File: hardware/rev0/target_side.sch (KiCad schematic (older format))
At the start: 4 parts, among them IC1 ECP5-BGA256

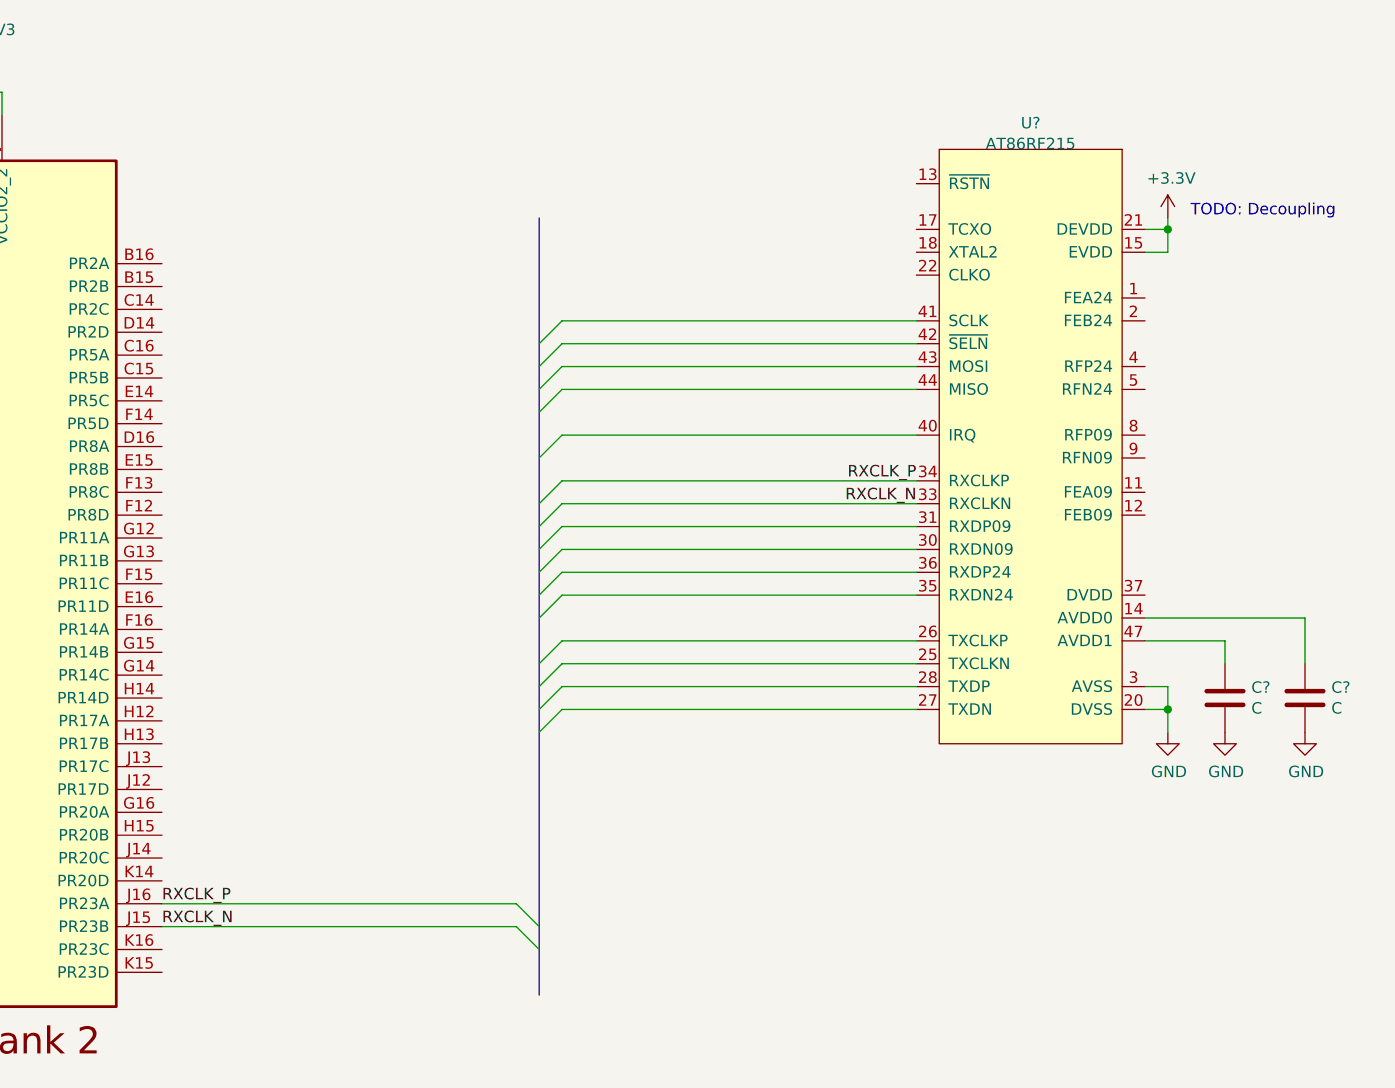
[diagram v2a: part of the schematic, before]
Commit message: Rough out LVDS
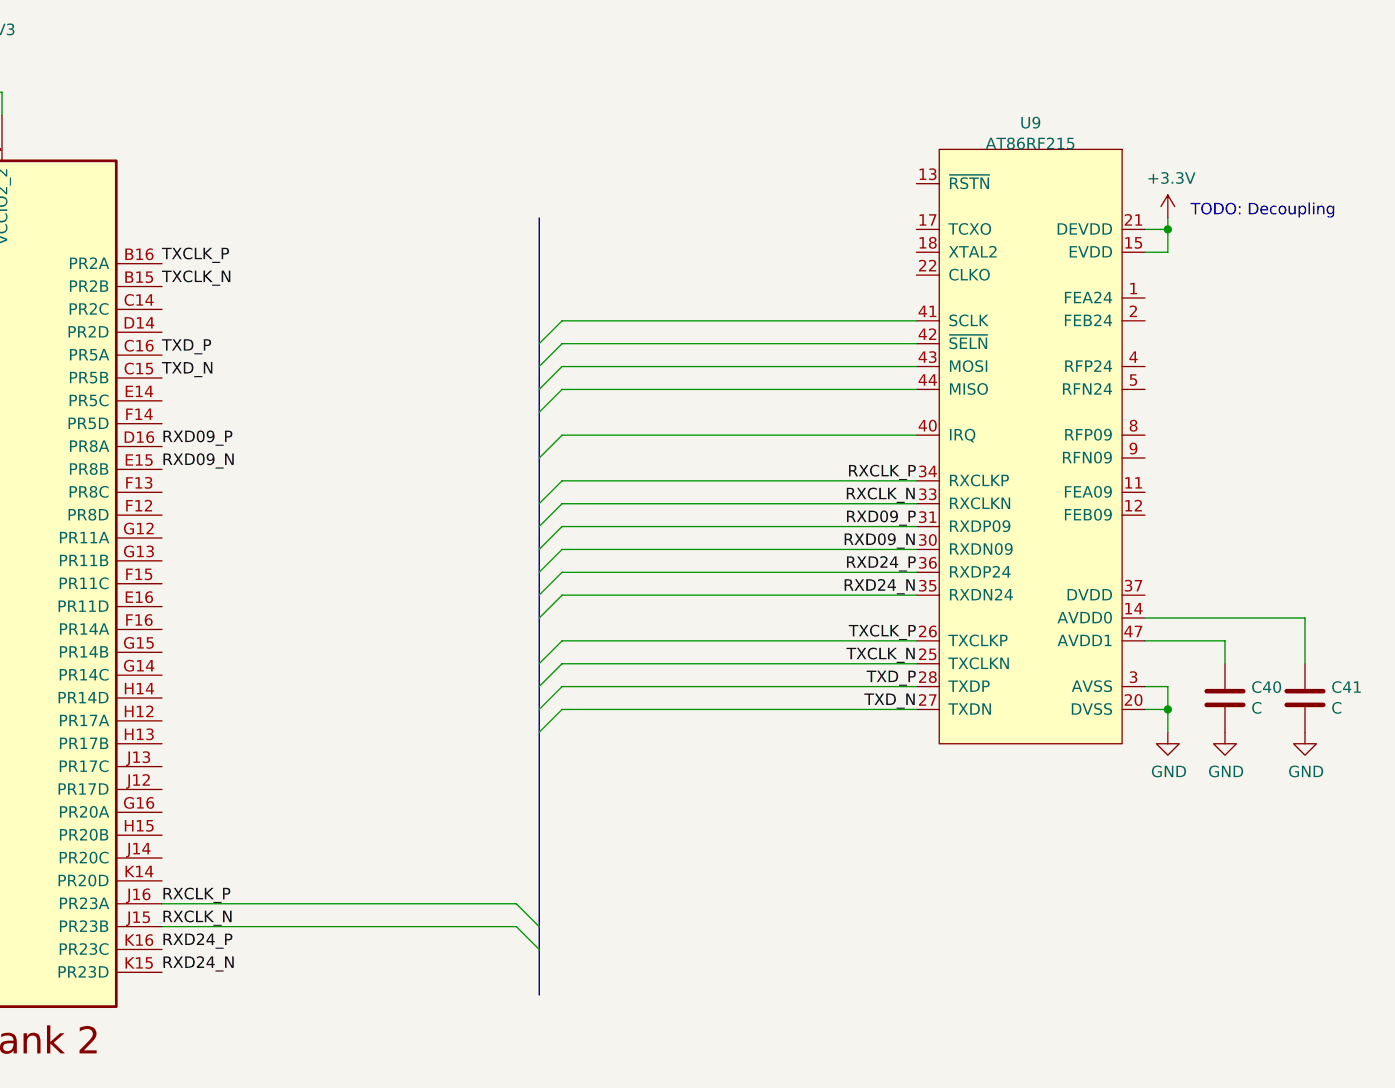
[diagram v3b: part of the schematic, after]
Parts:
- U9: renamed from U?; footprint (none) -> Package_DFN_QFN:QFN-48-1EP_7x7mm_P0.5mm_EP5.6x5.6mm
- gave numbers to parts that had none: 2
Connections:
- net TXCLK_N: now reaches IC1.B15 (PR2B)
- net TXCLK_N: now also U9.25 (TXCLKN)
- net TXCLK_P: now reaches IC1.B16 (PR2A)
- net TXCLK_P: now also U9.26 (TXCLKP)
- net TXD_N: now reaches IC1.C15 (PR5B)
- net TXD_N: now also U9.27 (TXDN)
- net TXD_P: now reaches IC1.C16 (PR5A)
- net TXD_P: now also U9.28 (TXDP)
- net RXD09_P: now reaches IC1.D16 (PR8A)
- net RXD09_P: now also U9.31 (RXDP09)
- net RXD09_N: now reaches IC1.E15 (PR8B)
- net RXD09_N: now also U9.30 (RXDN09)
- net RXD24_N: now reaches IC1.K15 (PR23D)
- net RXD24_N: now also U9.35 (RXDN24)
- net RXD24_P: now reaches IC1.K16 (PR23C)
- net RXD24_P: now also U9.36 (RXDP24)
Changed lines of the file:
@@
 Comment4 ""
 $EndDescr
+Wire Wire Line
+	1800 1900 1800 1800
+Wire Wire Line
+	1800 1800 1850 1800
+Wire Wire Line
+	1900 1800 1900 1900
+Wire Wire Line
+	1850 1800 1850 1700
+Connection ~ 1850 1800
+Wire Wire Line
+	1850 1800 1900 1800
+$Comp
+L power:+3V3 #PWR069
+U 1 1 5DE347EF
+P 1850 1700
+F 0 "#PWR069" H 1850 1550 50  0001 C CNN
+F 1 "+3V3" H 1864 1873 50  0000 C CNN
+F 2 "" H 1850 1700 50  0001 C CNN
+F 3 "" H 1850 1700 50  0001 C CNN
+	1    1850 1700
+	1    0    0    -1
+$EndComp
+$Comp
+L rf:AT86RF215 U9
+U 1 1 5E8BDF16
+P 6400 3350
+F 0 "U9" H 6400 4765 50  0000 C CNN
+F 1 "AT86RF215" H 6400 4674 50  0000 C CNN
+F 2 "Package_DFN_QFN:QFN-48-1EP_7x7mm_P0.5mm_EP5.6x5.6mm" H 6400 3100 50  0001 C CNN
+F 3 "" H 6400 3100 50  0001 C CNN
+	1    6400 3350
+	1    0    0    -1
+$EndComp
+Entry Wire Line
+	4250 3200 4350 3100
+Entry Wire Line
+	4250 3000 4350 2900
+Entry Wire Line
+	4250 2900 4350 2800
+Wire Wire Line
+	4350 2900 5900 2900
+Wire Wire Line
+	4350 2800 5900 2800
+Wire Wire Line
+	5900 3000 4350 3000
+Wire Wire Line
+	5900 3100 4350 3100
+Entry Wire Line
+	4350 3000 4250 3100
+Wire Wire Line
+	5900 3300 4350 3300
+Wire Wire Line
+	5900 3500 4350 3500
+Wire Wire Line
+	5900 3600 4350 3600
+Wire Wire Line
+	5900 3700 4350 3700
+Wire Wire Line
+	5900 3800 4350 3800
+Wire Wire Line
+	5900 3900 4350 3900
+Wire Wire Line
+	5900 4000 4350 4000
+Wire Wire Line
+	5900 4200 4350 4200
+Wire Wire Line
+	5900 4300 4350 4300
+Wire Wire Line
+	5900 4400 4350 4400
+Wire Wire Line
+	5900 4500 4350 4500
+Entry Wire Line
+	4250 3400 4350 3300
+Entry Wire Line
+	4250 3600 4350 3500
+Entry Wire Line
+	4250 3700 4350 3600
+Entry Wire Line
+	4250 3800 4350 3700
+Entry Wire Line
+	4250 3900 4350 3800
+Entry Wire Line
+	4250 4000 4350 3900
+Entry Wire Line
+	4250 4100 4350 4000
+Entry Wire Line
+	4250 4300 4350 4200
+Entry Wire Line
+	4250 4400 4350 4300
+Entry Wire Line
+	4250 4500 4350 4400
+Entry Wire Line
+	4250 4600 4350 4500
+$Comp
+L power:GND #PWR0109
+U 1 1 5E8DC56B
+P 7000 4600
+F 0 "#PWR0109" H 7000 4350 50  0001 C CNN
+F 1 "GND" H 7005 4427 50  0000 C CNN
+F 2 "" H 7000 4600 50  0001 C CNN
+F 3 "" H 7000 4600 50  0001 C CNN
+	1    7000 4600
+	1    0    0    -1
+$EndComp
+Wire Wire Line
+	6900 4500 7000 4500
+Wire Wire Line
+	7000 4500 7000 4600
+Wire Wire Line
+	6900 4400 7000 4400
+Wire Wire Line
+	7000 4400 7000 4500
+Connection ~ 7000 4500
+$Comp
+L Device:C C40
+U 1 1 5E8DD3C4
+P 7250 4450
+F 0 "C40" H 7365 4496 50  0000 L CNN
+F 1 "C" H 7365 4405 50  0000 L CNN
+F 2 "" H 7288 4300 50  0001 C CNN
+F 3 "~" H 7250 4450 50  0001 C CNN
+	1    7250 4450
+	1    0    0    -1
+$EndComp
+$Comp
+L Device:C C41
+U 1 1 5E8DDA59
+P 7600 4450
+F 0 "C41" H 7715 4496 50  0000 L CNN
+F 1 "C" H 7715 4405 50  0000 L CNN
+F 2 "" H 7638 4300 50  0001 C CNN
+F 3 "~" H 7600 4450 50  0001 C CNN
+	1    7600 4450
+	1    0    0    -1
+$EndComp
+$Comp
+L power:GND #PWR0117
+U 1 1 5E8DDC6A
+P 7250 4600
+F 0 "#PWR0117" H 7250 4350 50  0001 C CNN
+F 1 "GND" H 7255 4427 50  0000 C CNN
+F 2 "" H 7250 4600 50  0001 C CNN
+F 3 "" H 7250 4600 50  0001 C CNN
+	1    7250 4600
+	1    0    0    -1
+$EndComp
+$Comp
+L power:GND #PWR0122
+U 1 1 5E8DDD8B
+P 7600 4600
+F 0 "#PWR0122" H 7600 4350 50  0001 C CNN
+F 1 "GND" H 7605 4427 50  0000 C CNN
+F 2 "" H 7600 4600 50  0001 C CNN
+F 3 "" H 7600 4600 50  0001 C CNN
+	1    7600 4600
+	1    0    0    -1
+$EndComp
+Wire Wire Line
+	6900 4200 7250 4200
+Wire Wire Line
+	7250 4200 7250 4300
+Wire Wire Line
+	6900 4100 7600 4100
+Wire Wire Line
+	7600 4100 7600 4300
+$Comp
+L power:+3.3V #PWR0123
+U 1 1 5E8F94BD
+P 7000 2350
+F 0 "#PWR0123" H 7000 2200 50  0001 C CNN
+F 1 "+3.3V" H 7015 2523 50  0000 C CNN
+F 2 "" H 7000 2350 50  0001 C CNN
+F 3 "" H 7000 2350 50  0001 C CNN
+	1    7000 2350
+	1    0    0    -1
+$EndComp
+Wire Wire Line
+	6900 2400 7000 2400
+Wire Wire Line
+	7000 2400 7000 2350
+Wire Wire Line
+	6900 2500 7000 2500
+Wire Wire Line
+	7000 2500 7000 2400
+Connection ~ 7000 2400
+Text Notes 7100 2350 0    50   ~ 0
+TODO: Decoupling\n
+Text Label 5900 3500 2    50   ~ 0
+RXCLK_P
+Text Label 5900 3600 2    50   ~ 0
+RXCLK_N
+Text Notes 900  5550 0    50   ~ 0
+Clock inputs on:\n    PR23A/PR23B\n    PR23C/PR23D
+Text Label 2600 5350 0    50   ~ 0
+RXCLK_P
+Text Label 2600 5450 0    50   ~ 0
+RXCLK_N
+Wire Wire Line
+	2600 5350 4150 5350
+Wire Wire Line
+	2600 5450 4150 5450
+Entry Wire Line
+	4150 5350 4250 5450
+Entry Wire Line
+	4150 5450 4250 5550
+Text Label 5900 3700 2    50   ~ 0
+RXD09_P
+Text Label 5900 3800 2    50   ~ 0
+RXD09_N
+Text Label 5900 3900 2    50   ~ 0
+RXD24_P
+Text Label 5900 4000 2    50   ~ 0
+RXD24_N
+Text Label 5900 4200 2    50   ~ 0
+TXCLK_P
+Text Label 5900 4300 2    50   ~ 0
+TXCLK_N
+Text Label 5900 4400 2    50   ~ 0
+TXD_P
+Text Label 5900 4500 2    50   ~ 0
+TXD_N
+Text Label 2600 3350 0    50   ~ 0
+RXD09_P
+Text Label 2600 3450 0    50   ~ 0
+RXD09_N
+Text Label 2600 5550 0    50   ~ 0
+RXD24_P
+Text Label 2600 5650 0    50   ~ 0
+RXD24_N
+Text Label 2600 2550 0    50   ~ 0
+TXCLK_P
+Text Label 2600 2650 0    50   ~ 0
+TXCLK_N
+Text Label 2600 2950 0    50   ~ 0
+TXD_P
+Text Label 2600 3050 0    50   ~ 0
+TXD_N
 $Comp
 L fpgas_and_processors:ECP5-BGA256 IC1
@@
 	1    0    0    -1
 $EndComp
-Wire Wire Line
-	1800 1900 1800 1800
-Wire Wire Line
-	1800 1800 1850 1800
-Wire Wire Line
-	1900 1800 1900 1900
-Wire Wire Line
-	1850 1800 1850 1700
-Connection ~ 1850 1800
-Wire Wire Line
-	1850 1800 1900 1800
-$Comp
-L power:+3V3 #PWR069
-U 1 1 5DE347EF
-P 1850 1700
-F 0 "#PWR069" H 1850 1550 50  0001 C CNN
-F 1 "+3V3" H 1864 1873 50  0000 C CNN
-F 2 "" H 1850 1700 50  0001 C CNN
-F 3 "" H 1850 1700 50  0001 C CNN
-	1    1850 1700
-	1    0    0    -1
-$EndComp
-$Comp
-L rf:AT86RF215 U?
-U 1 1 5E8BDF16
-P 6400 3350
-F 0 "U?" H 6400 4765 50  0000 C CNN
-F 1 "AT86RF215" H 6400 4674 50  0000 C CNN
-F 2 "" H 6400 3100 50  0001 C CNN
-F 3 "" H 6400 3100 50  0001 C CNN
-	1    6400 3350
-	1    0    0    -1
-$EndComp
-Entry Wire Line
-	4250 3200 4350 3100
-Entry Wire Line
-	4250 3000 4350 2900
-Entry Wire Line
-	4250 2900 4350 2800
-Wire Wire Line
-	4350 2900 5900 2900
-Wire Wire Line
-	4350 2800 5900 2800
-Wire Wire Line
-	5900 3000 4350 3000
-Wire Wire Line
-	5900 3100 4350 3100
-Entry Wire Line
-	4350 3000 4250 3100
-Wire Wire Line
-	5900 3300 4350 3300
-Wire Wire Line
-	5900 3500 4350 3500
-Wire Wire Line
-	5900 3600 4350 3600
-Wire Wire Line
-	5900 3700 4350 3700
-Wire Wire Line
-	5900 3800 4350 3800
-Wire Wire Line
-	5900 3900 4350 3900
-Wire Wire Line
-	5900 4000 4350 4000
-Wire Wire Line
-	5900 4200 4350 4200
-Wire Wire Line
-	5900 4300 4350 4300
-Wire Wire Line
-	5900 4400 4350 4400
-Wire Wire Line
-	5900 4500 4350 4500
-Entry Wire Line
-	4250 3400 4350 3300
-Entry Wire Line
-	4250 3600 4350 3500
-Entry Wire Line
-	4250 3700 4350 3600
-Entry Wire Line
-	4250 3800 4350 3700
-Entry Wire Line
-	4250 3900 4350 3800
-Entry Wire Line
-	4250 4000 4350 3900
-Entry Wire Line
-	4250 4100 4350 4000
-Entry Wire Line
-	4250 4300 4350 4200
-Entry Wire Line
-	4250 4400 4350 4300
-Entry Wire Line
-	4250 4500 4350 4400
-Entry Wire Line
-	4250 4600 4350 4500
-$Comp
-L power:GND #PWR?
-U 1 1 5E8DC56B
-P 7000 4600
-F 0 "#PWR?" H 7000 4350 50  0001 C CNN
-F 1 "GND" H 7005 4427 50  0000 C CNN
-F 2 "" H 7000 4600 50  0001 C CNN
-F 3 "" H 7000 4600 50  0001 C CNN
-	1    7000 4600
-	1    0    0    -1
-$EndComp
-Wire Wire Line
-	6900 4500 7000 4500
-Wire Wire Line
-	7000 4500 7000 4600
-Wire Wire Line
-	6900 4400 7000 4400
-Wire Wire Line
-	7000 4400 7000 4500
-Connection ~ 7000 4500
-$Comp
-L Device:C C?
-U 1 1 5E8DD3C4
-P 7250 4450
-F 0 "C?" H 7365 4496 50  0000 L CNN
-F 1 "C" H 7365 4405 50  0000 L CNN
-F 2 "" H 7288 4300 50  0001 C CNN
-F 3 "~" H 7250 4450 50  0001 C CNN
-	1    7250 4450
-	1    0    0    -1
-$EndComp
-$Comp
-L Device:C C?
-U 1 1 5E8DDA59
-P 7600 4450
-F 0 "C?" H 7715 4496 50  0000 L CNN
-F 1 "C" H 7715 4405 50  0000 L CNN
-F 2 "" H 7638 4300 50  0001 C CNN
-F 3 "~" H 7600 4450 50  0001 C CNN
-	1    7600 4450
-	1    0    0    -1
-$EndComp
-$Comp
-L power:GND #PWR?
-U 1 1 5E8DDC6A
-P 7250 4600
-F 0 "#PWR?" H 7250 4350 50  0001 C CNN
-F 1 "GND" H 7255 4427 50  0000 C CNN
-F 2 "" H 7250 4600 50  0001 C CNN
-F 3 "" H 7250 4600 50  0001 C CNN
-	1    7250 4600
-	1    0    0    -1
-$EndComp
-$Comp
-L power:GND #PWR?
-U 1 1 5E8DDD8B
-P 7600 4600
-F 0 "#PWR?" H 7600 4350 50  0001 C CNN
-F 1 "GND" H 7605 4427 50  0000 C CNN
-F 2 "" H 7600 4600 50  0001 C CNN
-F 3 "" H 7600 4600 50  0001 C CNN
-	1    7600 4600
-	1    0    0    -1
-$EndComp
-Wire Wire Line
-	6900 4200 7250 4200
-Wire Wire Line
-	7250 4200 7250 4300
-Wire Wire Line
-	6900 4100 7600 4100
-Wire Wire Line
-	7600 4100 7600 4300
-$Comp
-L power:+3.3V #PWR?
-U 1 1 5E8F94BD
-P 7000 2350
-F 0 "#PWR?" H 7000 2200 50  0001 C CNN
-F 1 "+3.3V" H 7015 2523 50  0000 C CNN
-F 2 "" H 7000 2350 50  0001 C CNN
-F 3 "" H 7000 2350 50  0001 C CNN
-	1    7000 2350
-	1    0    0    -1
-$EndComp
-Wire Wire Line
-	6900 2400 7000 2400
-Wire Wire Line
-	7000 2400 7000 2350
-Wire Wire Line
-	6900 2500 7000 2500
-Wire Wire Line
-	7000 2500 7000 2400
-Connection ~ 7000 2400
-Text Notes 7100 2350 0    50   ~ 0
-TODO: Decoupling\n
-Text Label 5900 3500 2    50   ~ 0
-RXCLK_P
-Text Label 5900 3600 2    50   ~ 0
-RXCLK_N
-Text Notes 900  5550 0    50   ~ 0
-Clock inputs on:\n    PR23A/PR23B\n    PR23C/PR23D
-Text Label 2600 5350 0    50   ~ 0
-RXCLK_P
-Text Label 2600 5450 0    50   ~ 0
-RXCLK_N
-Wire Wire Line
-	2600 5350 4150 5350
-Wire Wire Line
-	2600 5450 4150 5450
 Wire Bus Line
 	4250 2350 4250 5750
-Entry Wire Line
-	4150 5350 4250 5450
-Entry Wire Line
-	4150 5450 4250 5550
 $EndSCHEMATC
